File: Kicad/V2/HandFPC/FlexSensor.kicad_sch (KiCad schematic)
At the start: 1 part

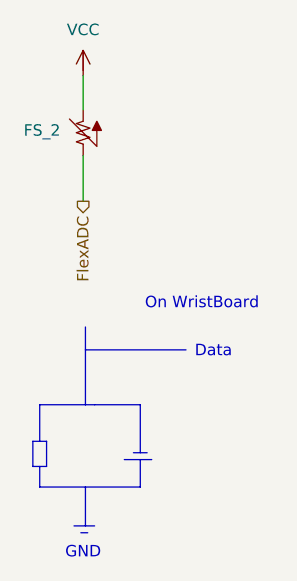
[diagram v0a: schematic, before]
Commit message: hand FPC pass erc no warning no error
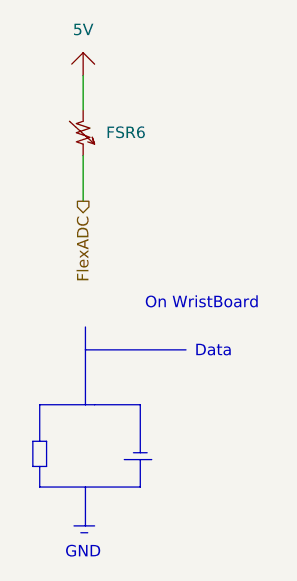
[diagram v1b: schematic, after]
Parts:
- removed FS_2: (no value), MyGlove:PinHeader_1x02_P2.54mm_Vertical, symbol G-Love:FS
- added FSR6: (no value), symbol G-Love-Symbols:FSR
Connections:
- net FlexADC: now also FSR6.1
- new net 5V: FSR6.2
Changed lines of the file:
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@@
 	)
 	(symbol
-		(lib_id "G-Love:FS")
-		(at 31.75 30.48 90)
-		(unit 1)
-		(body_style 1)
-		(exclude_from_sim no)
-		(in_bom no)
-		(on_board yes)
-		(in_pos_files yes)
-		(dnp no)
-		(property "Reference" "FS_2"
-			(at 27.178 30.226 90)
-			(show_name no)
-			(do_not_autoplace no)
-			(effects
-				(font
-					(size 1.27 1.27)
-				)
-			)
-		)
-		(property "Value" ""
-			(at 31.75 30.48 0)
-			(show_name no)
-			(do_not_autoplace no)
-			(effects
-				(font
-					(size 1.27 1.27)
-				)
-			)
-		)
-		(property "Footprint" "MyGlove:PinHeader_1x02_P2.54mm_Vertical"
-			(at 31.75 30.48 0)
-			(hide yes)
-			(show_name no)
-			(do_not_autoplace no)
-			(effects
-				(font
-					(size 1.27 1.27)
-				)
-			)
-		)
-		(property "Datasheet" "https://cdn.sparkfun.com/assets/8/e/7/a/0/flex22.pdf"
-			(at 40.132 26.924 0)
-			(hide yes)
-			(show_name no)
-			(do_not_autoplace no)
-			(effects
-				(font
-					(size 1.27 1.27)
-				)
-			)
-		)
-		(property "Description" "Flex Sensor Resistor"
-			(at 37.084 28.956 0)
-			(hide yes)
-			(show_name no)
-			(do_not_autoplace no)
-			(effects
-				(font
-					(size 1.27 1.27)
-				)
-			)
-		)
-		(property "Minimum quantity per command" ""
-			(at 31.75 30.48 90)
-			(hide yes)
-			(show_name no)
-			(do_not_autoplace no)
-			(effects
-				(font
-					(size 1.27 1.27)
-				)
-			)
-		)
-		(pin "2"
-		)
-		(pin "1"
-		)
-		(instances
-			(project "HandFPC"
-				(path "/7221f3d8-f3bc-4a50-a6fd-69c2d8ca27db/0b1bb178-9530-4748-8b07-933fe0c8d524"
-					(reference "FS_2")
-					(unit 1)
-				)
-				(path "/7221f3d8-f3bc-4a50-a6fd-69c2d8ca27db/7a2974e5-124b-4db5-8e90-e949fd9545a7"
-					(reference "FS_1")
-					(unit 1)
-				)
-				(path "/7221f3d8-f3bc-4a50-a6fd-69c2d8ca27db/93c35869-ca7a-4596-991e-6eeeacdf1f70"
-					(reference "FS_1")
-					(unit 1)
-				)
-				(path "/7221f3d8-f3bc-4a50-a6fd-69c2d8ca27db/a00bc8a6-48ba-4c2b-a585-b9390a223b1c"
-					(reference "FS_1")
-					(unit 1)
-				)
-				(path "/7221f3d8-f3bc-4a50-a6fd-69c2d8ca27db/d64adc8c-2a84-4c15-a7c4-b37086fe5b0e"
-					(reference "FS_1")
-					(unit 1)
-				)
-			)
-		)
-	)
-	(symbol
-		(lib_id "G-Love:VCC")
-		(at 31.75 22.86 0)
+		(lib_id "G-Love-Symbols:+5V")
+		(at 31.75 21.59 0)
 		(unit 1)
 		(body_style 1)
@@
 		(dnp no)
 		(fields_autoplaced yes)
-		(property "Reference" "#PWR013"
-			(at 35.56 24.638 0)
+		(property "Reference" "#PWR011"
+			(at 34.29 20.9549 0)
 			(hide yes)
 			(show_name no)
@@
 					(size 1.27 1.27)
 				)
+				(justify left)
 			)
 		)
-		(property "Value" "VCC"
+		(property "Value" "5V"
 			(at 31.75 19.05 0)
 			(show_name no)
@@
 		)
 		(property "Footprint" ""
-			(at 31.75 22.86 0)
+			(at 31.75 21.59 0)
 			(hide yes)
 			(show_name no)
@@
 		)
 		(property "Datasheet" ""
-			(at 31.75 22.86 0)
+			(at 31.75 21.59 0)
 			(hide yes)
 			(show_name no)
@@
 		)
 		(property "Description" ""
-			(at 31.75 22.86 0)
+			(at 31.75 21.59 0)
 			(hide yes)
 			(show_name no)
@@
 			(project "HandFPC"
 				(path "/7221f3d8-f3bc-4a50-a6fd-69c2d8ca27db/0b1bb178-9530-4748-8b07-933fe0c8d524"
-					(reference "#PWR013")
+					(reference "#PWR011")
 					(unit 1)
 				)
 				(path "/7221f3d8-f3bc-4a50-a6fd-69c2d8ca27db/7a2974e5-124b-4db5-8e90-e949fd9545a7"
-					(reference "#PWR012")
+					(reference "#PWR018")
 					(unit 1)
 				)
 				(path "/7221f3d8-f3bc-4a50-a6fd-69c2d8ca27db/93c35869-ca7a-4596-991e-6eeeacdf1f70"
-					(reference "#PWR012")
+					(reference "#PWR020")
 					(unit 1)
 				)
 				(path "/7221f3d8-f3bc-4a50-a6fd-69c2d8ca27db/a00bc8a6-48ba-4c2b-a585-b9390a223b1c"
-					(reference "#PWR012")
+					(reference "#PWR019")
 					(unit 1)
 				)
 				(path "/7221f3d8-f3bc-4a50-a6fd-69c2d8ca27db/d64adc8c-2a84-4c15-a7c4-b37086fe5b0e"
-					(reference "#PWR012")
+					(reference "#PWR017")
 					(unit 1)
 				)
+			)
+		)
+	)
+	(symbol
+		(lib_id "G-Love-Symbols:FSR")
+		(at 31.75 30.48 90)
+		(unit 1)
+		(body_style 1)
+		(exclude_from_sim no)
+		(in_bom yes)
+		(on_board yes)
+		(in_pos_files yes)
+		(dnp no)
+		(fields_autoplaced yes)
+		(property "Reference" "FSR6"
+			(at 34.29 30.4799 90)
+			(show_name no)
+			(do_not_autoplace no)
+			(effects
+				(font
+					(size 1.27 1.27)
+				)
+				(justify right)
+			)
+		)
+		(property "Value" ""
+			(at 31.75 30.48 0)
+			(show_name no)
+			(do_not_autoplace no)
+			(effects
+				(font
+					(size 1.27 1.27)
+				)
+			)
+		)
+		(property "Footprint" ""
+			(at 31.75 30.48 0)
+			(hide yes)
+			(show_name no)
+			(do_not_autoplace no)
+			(effects
+				(font
+					(size 1.27 1.27)
+				)
+			)
+		)
+		(property "Datasheet" "https://cdn.sparkfun.com/assets/8/a/1/2/0/2010-10-26-DataSheet-FSR402-Layout2.pdf"
+			(at 40.132 26.924 0)
+			(hide yes)
+			(show_name no)
+			(do_not_autoplace no)
+			(effects
+				(font
+					(size 1.27 1.27)
+				)
+			)
+		)
+		(property "Description" "Touch Force Sensor Resistor"
+			(at 37.084 28.956 0)
+			(hide yes)
+			(show_name no)
+			(do_not_autoplace no)
+			(effects
+				(font
+					(size 1.27 1.27)
+				)
+			)
+		)
+		(pin "1"
+		)
+		(pin "2"
+		)
+		(instances
+			(project "HandFPC"
+				(path "/7221f3d8-f3bc-4a50-a6fd-69c2d8ca27db/0b1bb178-9530-4748-8b07-933fe0c8d524"
+					(reference "FSR6")
+					(unit 1)
+				)
+				(path "/7221f3d8-f3bc-4a50-a6fd-69c2d8ca27db/7a2974e5-124b-4db5-8e90-e949fd9545a7"
+					(reference "FSR8")
+					(unit 1)
+				)
+				(path "/7221f3d8-f3bc-4a50-a6fd-69c2d8ca27db/93c35869-ca7a-4596-991e-6eeeacdf1f70"
+					(reference "FSR10")
+					(unit 1)
+				)
+				(path "/7221f3d8-f3bc-4a50-a6fd-69c2d8ca27db/a00bc8a6-48ba-4c2b-a585-b9390a223b1c"
+					(reference "FSR9")
+					(unit 1)
+				)
+				(path "/7221f3d8-f3bc-4a50-a6fd-69c2d8ca27db/d64adc8c-2a84-4c15-a7c4-b37086fe5b0e"
+					(reference "FSR7")
+					(unit 1)
+				)

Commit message: add custom symbol for FPC connector
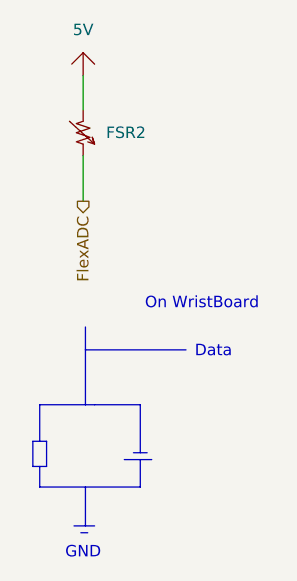
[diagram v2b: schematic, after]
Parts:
- renumbered FSR6 to FSR2
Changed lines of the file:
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@@
 		(dnp no)
 		(fields_autoplaced yes)
-		(property "Reference" "#PWR011"
+		(property "Reference" "#PWR013"
 			(at 34.29 20.9549 0)
 			(hide yes)
@@
 			(project "HandFPC"
 				(path "/7221f3d8-f3bc-4a50-a6fd-69c2d8ca27db/0b1bb178-9530-4748-8b07-933fe0c8d524"
-					(reference "#PWR011")
+					(reference "#PWR013")
 					(unit 1)
 				)
 				(path "/7221f3d8-f3bc-4a50-a6fd-69c2d8ca27db/7a2974e5-124b-4db5-8e90-e949fd9545a7"
+					(reference "#PWR017")
+					(unit 1)
+				)
+				(path "/7221f3d8-f3bc-4a50-a6fd-69c2d8ca27db/93c35869-ca7a-4596-991e-6eeeacdf1f70"
+					(reference "#PWR019")
+					(unit 1)
+				)
+				(path "/7221f3d8-f3bc-4a50-a6fd-69c2d8ca27db/a00bc8a6-48ba-4c2b-a585-b9390a223b1c"
 					(reference "#PWR018")
 					(unit 1)
 				)
-				(path "/7221f3d8-f3bc-4a50-a6fd-69c2d8ca27db/93c35869-ca7a-4596-991e-6eeeacdf1f70"
-					(reference "#PWR020")
-					(unit 1)
-				)
-				(path "/7221f3d8-f3bc-4a50-a6fd-69c2d8ca27db/a00bc8a6-48ba-4c2b-a585-b9390a223b1c"
-					(reference "#PWR019")
-					(unit 1)
-				)
 				(path "/7221f3d8-f3bc-4a50-a6fd-69c2d8ca27db/d64adc8c-2a84-4c15-a7c4-b37086fe5b0e"
-					(reference "#PWR017")
+					(reference "#PWR016")
 					(unit 1)
 				)
@@
 		(dnp no)
 		(fields_autoplaced yes)
-		(property "Reference" "FSR6"
+		(property "Reference" "FSR2"
 			(at 34.29 30.4799 90)
 			(show_name no)
@@
 			(project "HandFPC"
 				(path "/7221f3d8-f3bc-4a50-a6fd-69c2d8ca27db/0b1bb178-9530-4748-8b07-933fe0c8d524"
+					(reference "FSR2")
+					(unit 1)
+				)
+				(path "/7221f3d8-f3bc-4a50-a6fd-69c2d8ca27db/7a2974e5-124b-4db5-8e90-e949fd9545a7"
+					(reference "FSR4")
+					(unit 1)
+				)
+				(path "/7221f3d8-f3bc-4a50-a6fd-69c2d8ca27db/93c35869-ca7a-4596-991e-6eeeacdf1f70"
 					(reference "FSR6")
 					(unit 1)
 				)
-				(path "/7221f3d8-f3bc-4a50-a6fd-69c2d8ca27db/7a2974e5-124b-4db5-8e90-e949fd9545a7"
-					(reference "FSR8")
-					(unit 1)
-				)
-				(path "/7221f3d8-f3bc-4a50-a6fd-69c2d8ca27db/93c35869-ca7a-4596-991e-6eeeacdf1f70"
-					(reference "FSR10")
-					(unit 1)
-				)
 				(path "/7221f3d8-f3bc-4a50-a6fd-69c2d8ca27db/a00bc8a6-48ba-4c2b-a585-b9390a223b1c"
-					(reference "FSR9")
+					(reference "FSR5")
 					(unit 1)
 				)
 				(path "/7221f3d8-f3bc-4a50-a6fd-69c2d8ca27db/d64adc8c-2a84-4c15-a7c4-b37086fe5b0e"
-					(reference "FSR7")
+					(reference "FSR3")
 					(unit 1)
 				)

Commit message: fix flex sensor mixed up with force sensor
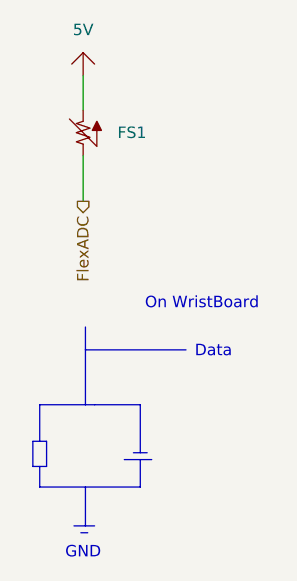
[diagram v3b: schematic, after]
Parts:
- removed FSR2: (no value), symbol G-Love-Symbols:FSR
- added FS1: (no value), symbol G-Love-Symbols:FS
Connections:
- net 5V: now also FS1.2
- net FlexADC: now also FS1.1
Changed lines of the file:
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@@
 	)
 	(symbol
-		(lib_id "G-Love-Symbols:FSR")
+		(lib_id "G-Love-Symbols:FS")
 		(at 31.75 30.48 90)
 		(unit 1)
@@
 		(dnp no)
 		(fields_autoplaced yes)
-		(property "Reference" "FSR2"
-			(at 34.29 30.4799 90)
+		(property "Reference" "FS1"
+			(at 35.56 30.4799 90)
 			(show_name no)
 			(do_not_autoplace no)
@@
 			)
 		)
-		(property "Datasheet" "https://cdn.sparkfun.com/assets/8/a/1/2/0/2010-10-26-DataSheet-FSR402-Layout2.pdf"
+		(property "Datasheet" "https://cdn.sparkfun.com/assets/8/e/7/a/0/flex22.pdf"
 			(at 40.132 26.924 0)
 			(hide yes)
@@
 			)
 		)
-		(property "Description" "Touch Force Sensor Resistor"
+		(property "Description" "Flex Sensor Resistor"
 			(at 37.084 28.956 0)
 			(hide yes)
@@
 			)
 		)
+		(pin "2"
+		)
 		(pin "1"
-		)
-		(pin "2"
 		)
 		(instances
 			(project "HandFPC"
 				(path "/7221f3d8-f3bc-4a50-a6fd-69c2d8ca27db/0b1bb178-9530-4748-8b07-933fe0c8d524"
-					(reference "FSR2")
+					(reference "FS1")
 					(unit 1)
 				)
 				(path "/7221f3d8-f3bc-4a50-a6fd-69c2d8ca27db/7a2974e5-124b-4db5-8e90-e949fd9545a7"
-					(reference "FSR4")
+					(reference "FS3")
 					(unit 1)
 				)
 				(path "/7221f3d8-f3bc-4a50-a6fd-69c2d8ca27db/93c35869-ca7a-4596-991e-6eeeacdf1f70"
-					(reference "FSR6")
+					(reference "FS5")
 					(unit 1)
 				)
 				(path "/7221f3d8-f3bc-4a50-a6fd-69c2d8ca27db/a00bc8a6-48ba-4c2b-a585-b9390a223b1c"
-					(reference "FSR5")
+					(reference "FS4")
 					(unit 1)
 				)
 				(path "/7221f3d8-f3bc-4a50-a6fd-69c2d8ca27db/d64adc8c-2a84-4c15-a7c4-b37086fe5b0e"
-					(reference "FSR3")
+					(reference "FS2")
 					(unit 1)
 				)

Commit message: add FPC footprints
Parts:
- FS1: footprint (none) -> MyGlove:FPC_FS
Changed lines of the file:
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@@
 			)
 		)
-		(property "Footprint" ""
+		(property "Footprint" "MyGlove:FPC_FS"
 			(at 31.75 30.48 0)
 			(hide yes)

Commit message: add routing
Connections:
- net 5V renamed +3.3V
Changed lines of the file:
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@@
 	)
 	(symbol
-		(lib_id "G-Love-Symbols:+5V")
-		(at 31.75 21.59 0)
+		(lib_id "G-Love-Symbols:+3.3V")
+		(at 31.75 22.86 0)
 		(unit 1)
 		(body_style 1)
@@
 		(in_pos_files yes)
 		(dnp no)
-		(fields_autoplaced yes)
-		(property "Reference" "#PWR013"
-			(at 34.29 20.9549 0)
+		(property "Reference" "#PWR04"
+			(at 35.56 24.638 0)
 			(hide yes)
 			(show_name no)
@@
 					(size 1.27 1.27)
 				)
-				(justify left)
 			)
 		)
-		(property "Value" "5V"
-			(at 31.75 19.05 0)
+		(property "Value" "+3.3V"
+			(at 35.052 21.336 0)
 			(show_name no)
 			(do_not_autoplace no)
@@
 		)
 		(property "Footprint" ""
-			(at 31.75 21.59 0)
+			(at 31.75 22.86 0)
 			(hide yes)
 			(show_name no)
@@
 		)
 		(property "Datasheet" ""
-			(at 31.75 21.59 0)
+			(at 31.75 22.86 0)
 			(hide yes)
 			(show_name no)
@@
 		)
 		(property "Description" ""
-			(at 31.75 21.59 0)
+			(at 31.75 22.86 0)
 			(hide yes)
 			(show_name no)
@@
 			(project "HandFPC"
 				(path "/7221f3d8-f3bc-4a50-a6fd-69c2d8ca27db/0b1bb178-9530-4748-8b07-933fe0c8d524"
+					(reference "#PWR04")
+					(unit 1)
+				)
+				(path "/7221f3d8-f3bc-4a50-a6fd-69c2d8ca27db/7a2974e5-124b-4db5-8e90-e949fd9545a7"
 					(reference "#PWR013")
 					(unit 1)
 				)
-				(path "/7221f3d8-f3bc-4a50-a6fd-69c2d8ca27db/7a2974e5-124b-4db5-8e90-e949fd9545a7"
+				(path "/7221f3d8-f3bc-4a50-a6fd-69c2d8ca27db/93c35869-ca7a-4596-991e-6eeeacdf1f70"
 					(reference "#PWR017")
 					(unit 1)
 				)
-				(path "/7221f3d8-f3bc-4a50-a6fd-69c2d8ca27db/93c35869-ca7a-4596-991e-6eeeacdf1f70"
-					(reference "#PWR019")
-					(unit 1)
-				)
 				(path "/7221f3d8-f3bc-4a50-a6fd-69c2d8ca27db/a00bc8a6-48ba-4c2b-a585-b9390a223b1c"
-					(reference "#PWR018")
+					(reference "#PWR016")
 					(unit 1)
 				)
 				(path "/7221f3d8-f3bc-4a50-a6fd-69c2d8ca27db/d64adc8c-2a84-4c15-a7c4-b37086fe5b0e"
-					(reference "#PWR016")
+					(reference "#PWR06")
 					(unit 1)
 				)
